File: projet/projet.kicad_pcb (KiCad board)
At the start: 2 copper layers, 2 parts, among them U1 RASPBERRY_PI_PICO

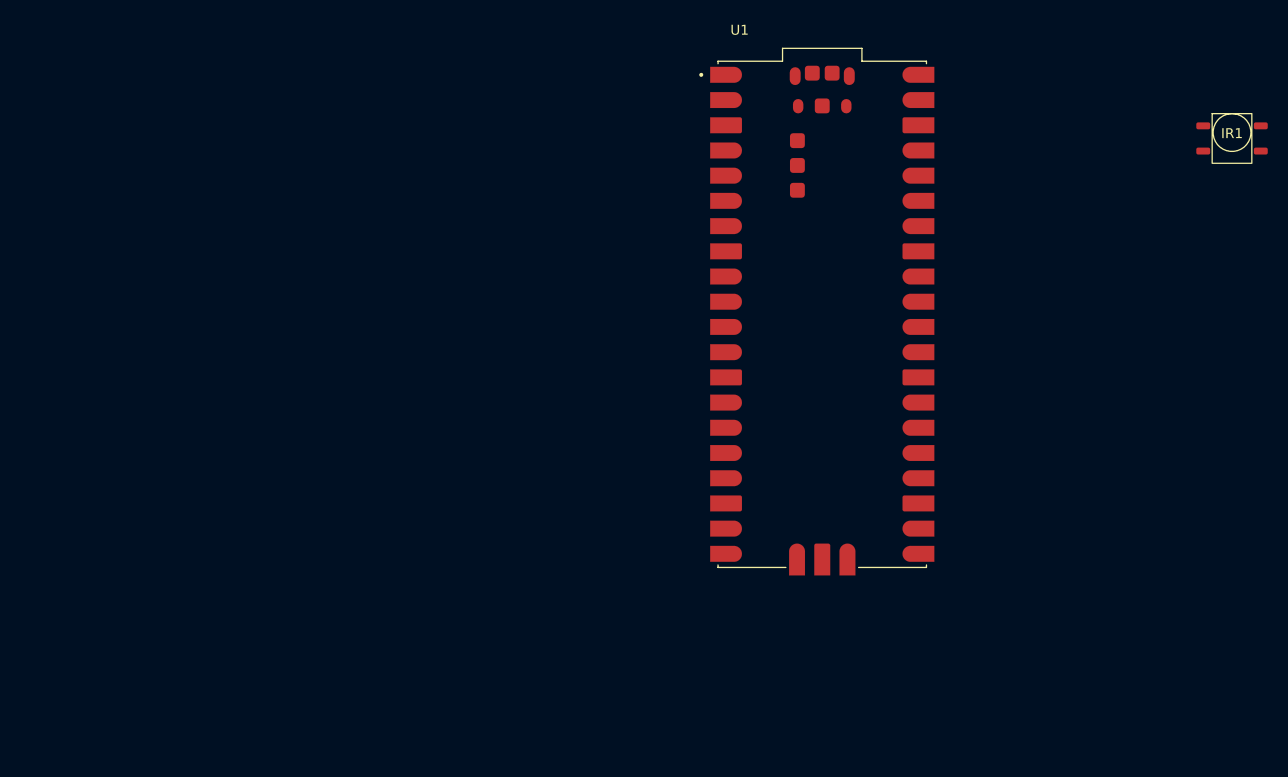
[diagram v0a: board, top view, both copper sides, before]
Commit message: début Routage
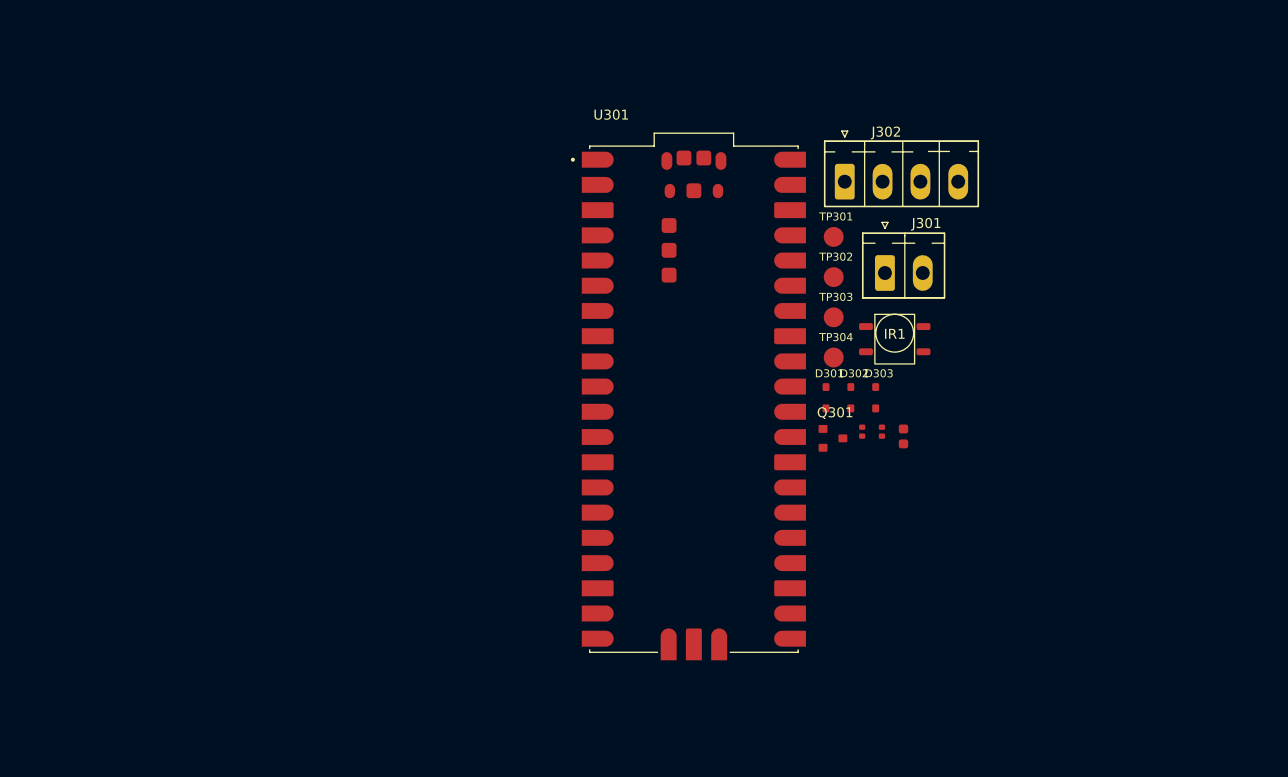
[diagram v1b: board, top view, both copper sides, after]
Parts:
- removed U1: RASPBERRY_PI_PICO, codium_Modules:Raspberry-Pi-Pico
- added C301: 10uF 10V, codium_Basics:C0603, F.Cu at (139.0, 87.8)
- added D301: TVS 5V, codium_Basics:SOD323_NP, F.Cu at (131.2, 83.8)
- added D302: TVS 5V, codium_Basics:SOD323_NP, F.Cu at (133.7, 83.8)
- added D303: TVS 5V, codium_Basics:SOD323_NP, F.Cu at (136.2, 83.8)
- added J301: EMB_P3.81_1x02_VERTICAL, codium_Connectors:Conn_THT_3.81_2x1_Vertical, F.Cu at (137.1, 71.3)
- added J302: EMB_P3.81_1x04_VERTICAL, codium_Connectors:Conn_THT_3.81_4x1_Vertical, F.Cu at (133.1, 62.1)
- added Q301: MOS P 20V 2A, codium_Basics:SOT23, F.Cu at (131.9, 87.9)
- added R301: 100R, codium_Basics:R0402, F.Cu at (134.8, 87.3)
- added R302: 100k, codium_Basics:R0402, F.Cu at (136.8, 87.3)
- added TP301: TestGND, codium_Pads:TestPoint_Pad_D2.0mm, F.Cu at (132.0, 67.7)
- added TP302: TestVCC, codium_Pads:TestPoint_Pad_D2.0mm, F.Cu at (132.0, 71.7)
- added TP303: TestCapteur, codium_Pads:TestPoint_Pad_D2.0mm, F.Cu at (132.0, 75.8)
- added TP304: TestLED, codium_Pads:TestPoint_Pad_D2.0mm, F.Cu at (132.0, 79.8)
- added U301: Raspberry-Pi-Pico_Linked, codium_Modules:Raspberry-Pi-Pico, F.Cu at (117.9, 84.0)
- moved IR1 39.5 mm to (138.1, 78.0)
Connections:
- net Net-(IR1-GND-Pad1) renamed GND
- IR1 pad 3: unconnected-(IR1-OUT-Pad3) -> lecteur_ir_13
- IR1 pad 4: unconnected-(IR1-VCC-Pad4) -> Net-(IR1-VCC)

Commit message: démarrage routage et installations des ports
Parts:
- added C302: 10uF 10V, codium_Basics:C0603, F.Cu at (91.6, 92.0)
- moved Q301 61.1 mm to (79.5, 56.5)
- moved J302 54.8 mm to (96.5, 102.9), turned to 180 degrees
- moved U301 54.2 mm to (64.0, 78.5)
- moved J301 50.2 mm to (89.2, 56.5)
- moved TP302 49.7 mm to (84.6, 56.5)
- moved TP304 48.0 mm to (86.8, 96.0)
- moved D301 46.2 mm to (91.0, 61.0), turned to 90 degrees
- moved D303 45.8 mm to (91.6, 94.2), turned to -90 degrees
- moved D302 43.9 mm to (91.5, 96.0), turned to 90 degrees
- moved TP301 36.2 mm to (97.6, 56.4)
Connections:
- U301 pad A: unconnected-(U301-USB_SHIELD-PadA) -> GND
- U301 pad B: unconnected-(U301-USB_SHIELD-PadA)_2 -> GND
- U301 pad C: unconnected-(U301-USB_SHIELD-PadA)_3 -> GND
- U301 pad D: unconnected-(U301-USB_SHIELD-PadA)_1 -> GND
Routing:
- net +5V: track 0.00 -> 95.0 mm
- net ruban_led_7: track 0.00 -> 84.4 mm
- net GND: track 0.00 -> 80.3 mm, vias 0 -> 12
- net vbus: track 0.00 -> 5.30 mm
- net vsys: track 0.00 -> 5.03 mm
- added copper zone on B.Cu, net GND
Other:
- board outline added: 50 x 70 mm

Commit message: Première version carte complète
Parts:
- added F301: 1.1A, codium_Basics:R1812L, F.Cu at (84.6, 62.9)
- moved IR1 55.8 mm to (82.8, 70.8)
- moved R302 50.2 mm to (86.8, 84.0), turned to 90 degrees
- moved C301 49.9 mm to (90.1, 78.2), turned to 90 degrees
- moved TP303 49.2 mm to (82.8, 75.6)
- moved R301 44.5 mm to (90.8, 81.0)
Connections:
- C302 pad 1: +5V -> Net-(IR1-VCC)
- D301 pad 1: +5V -> Net-(D301-A1)
- D303 pad 2: +5V -> Net-(IR1-VCC)
- J301 pad 1: +5V -> Net-(D301-A1)
- J302 pad 4: +5V -> Net-(IR1-VCC)
- Q301 pad 3: +5V -> Net-(IR1-VCC)
- R301 pad 2: +5V -> Net-(IR1-VCC)
- R302 pad 2: +5V -> Net-(IR1-VCC)
- TP302 pad 1: +5V -> Net-(D301-A1)
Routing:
- net Net-(IR1-VCC): track 0.00 -> 118.9 mm
- net +5V: track 95.0 -> 0.00 mm
- net lecteur_ir_13: track 0.00 -> 73.0 mm
- net Net-(D301-A1): track 0.00 -> 17.4 mm
- net GND: track 80.3 -> 86.8 mm, vias 12 -> 14

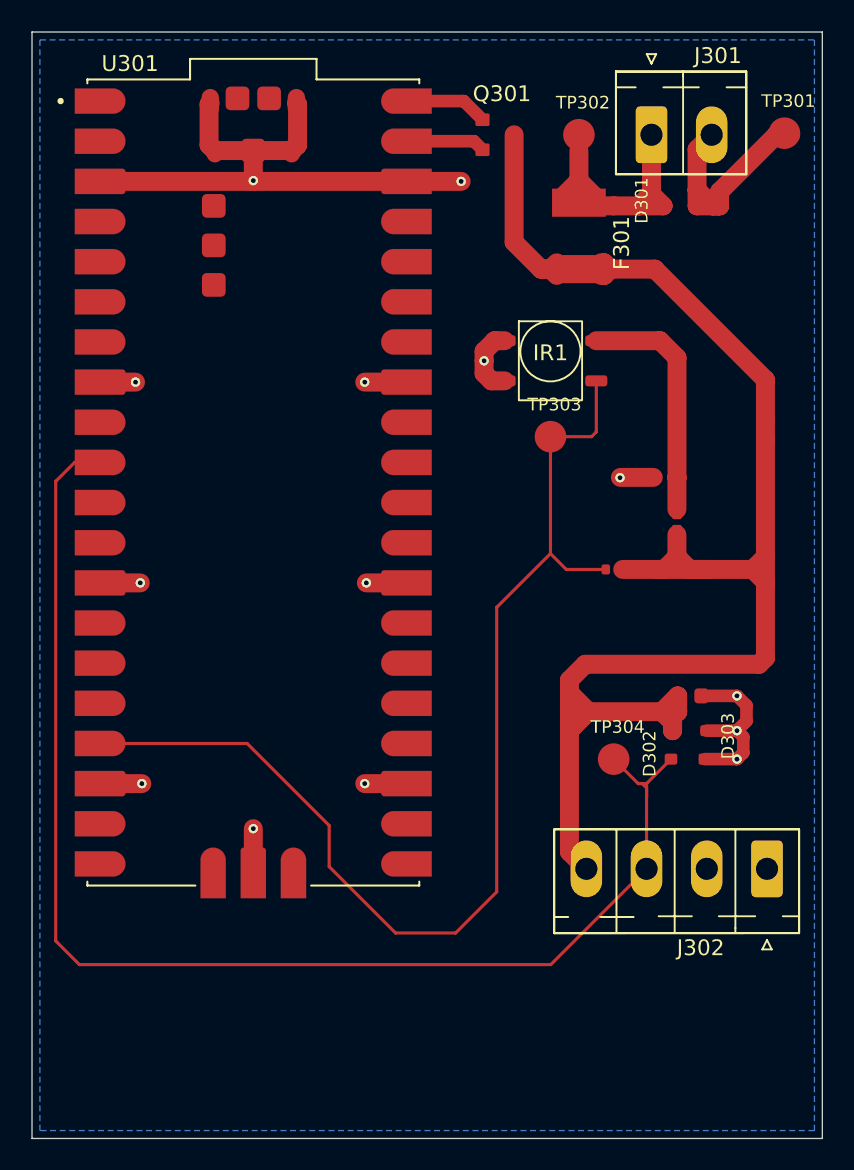
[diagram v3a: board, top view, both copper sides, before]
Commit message: Correctif des pistes et plan de masse au front
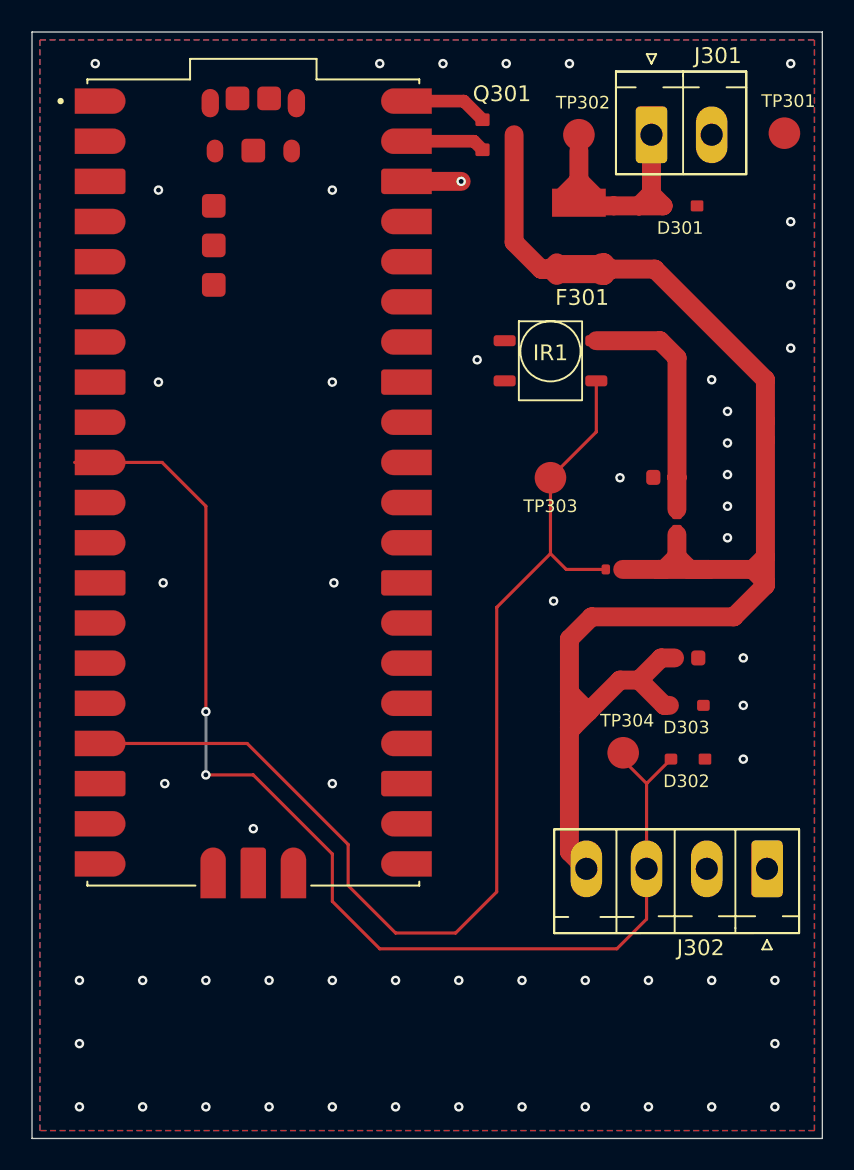
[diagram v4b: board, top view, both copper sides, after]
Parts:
- moved TP303 2.60 mm to (82.8, 78.2)
- moved C302 2.41 mm to (91.4, 89.6)
- moved D303 1.61 mm to (91.4, 92.6)
- moved TP304 0.72 mm to (87.4, 95.6)
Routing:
- net GND: track 86.8 -> 3.49 mm, vias 14 -> 57
- net ruban_led_7: track 84.4 -> 74.7 mm, vias 0 -> 2
- net Net-(IR1-VCC): track 118.9 -> 116.2 mm
- net lecteur_ir_13: track 73.0 -> 71.5 mm
- added copper zone on F.Cu, net GND
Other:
- board text added: "No computer were harmed in the conception of this card"

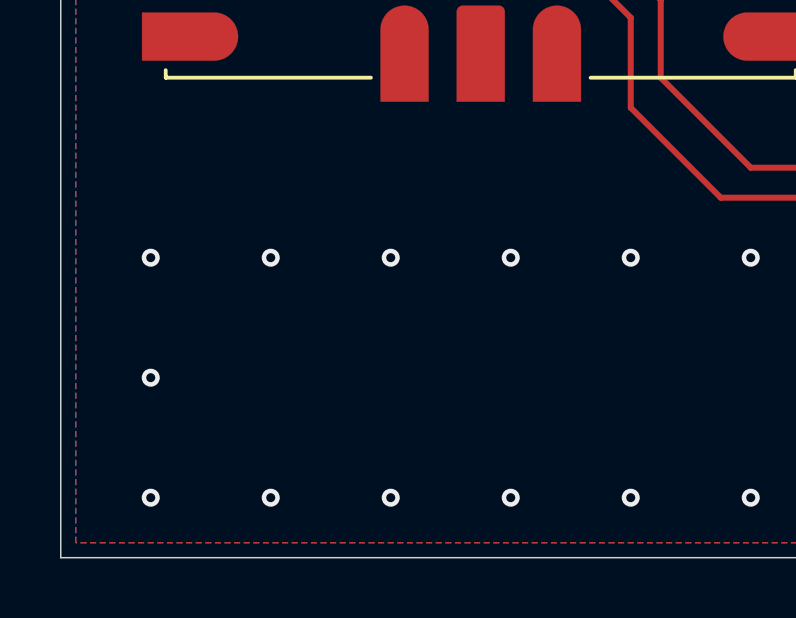
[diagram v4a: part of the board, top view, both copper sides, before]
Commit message: ajout des images sur le^pcb
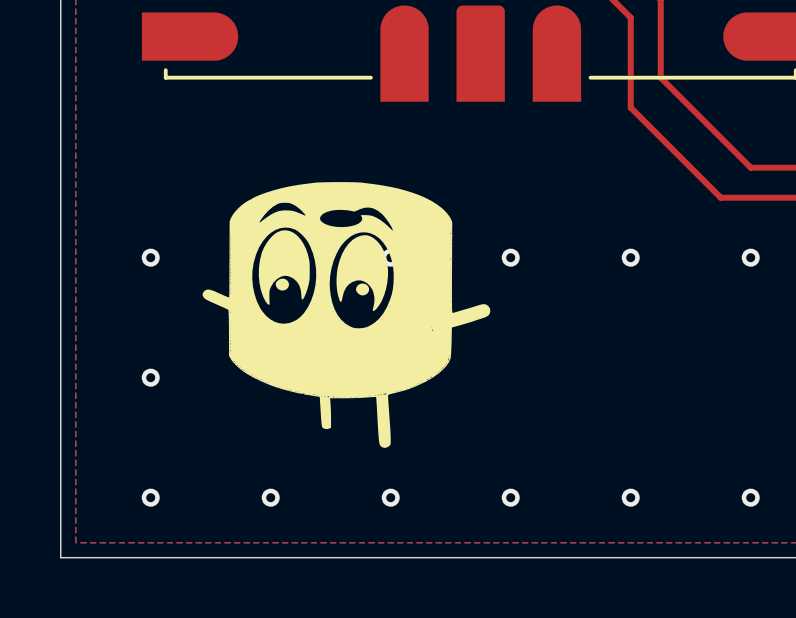
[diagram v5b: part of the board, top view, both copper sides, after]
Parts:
- added G***: LOGO, LOGO, F.Cu at (59.5, 112.0)
- added G***: LOGO, LOGO, B.Cu at (77.0, 68.0)
- added G***: LOGO, LOGO, B.Cu at (75.0, 86.0)

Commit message: Ajout de graphisme et fichiers de fabrications
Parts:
- moved G*** 2.00 mm to (75.0, 68.0)
- moved G*** 1.12 mm to (59.0, 113.0)
- renumbered C302 to C301, C301 to C302, IR1 to IR301, R302 to R301, R301 to R302, TP302 to TP301, TP301 to TP302, TP304 to TP303, TP303 to TP304
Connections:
- C301 pad 1: Net-(IR1-VCC) -> +5V
- C302 pad 2: Net-(IR1-VCC) -> Net-(IR301-VCC)
- D303 pad 2: Net-(IR1-VCC) -> +5V
- F301 pad 2: Net-(IR1-VCC) -> +5V
- IR301 pad 4: Net-(IR1-VCC) -> Net-(IR301-VCC)
- J302 pad 4: Net-(IR1-VCC) -> +5V
- Q301 pad 3: Net-(IR1-VCC) -> +5V
- R301 pad 2: Net-(IR1-VCC) -> +5V
- R302 pad 1: Net-(IR1-VCC) -> Net-(IR301-VCC)
- R302 pad 2: Net-(IR1-VCC) -> +5V
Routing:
- net Net-(IR1-VCC): track 116.2 -> 0.00 mm
- net +5V: track 0.00 -> 101.1 mm
- net Net-(IR301-VCC): track 0.00 -> 15.1 mm
- net GND: vias 57 -> 60
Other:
- board text added: "Design proposed by Gaël Chauvet & Lucas Hyot"

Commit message: Dernière modifs avant vérif externes
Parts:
- added D304: LED GREEN, codium_Leds:LED0805, F.Cu at (96.4, 66.0)
- added D305: LED GREEN, codium_Leds:LED0805, F.Cu at (78.9, 94.0)
- added D306: LED GREEN, codium_Leds:LED0805, F.Cu at (79.1, 90.0)
- added D307: LED GREEN, codium_Leds:LED0805, F.Cu at (79.2, 86.0)
- added R303: 330R, codium_Basics:R0603, F.Cu at (96.4, 62.2)
- added R304: 330R, codium_Basics:R0603, F.Cu at (82.8, 94.0)
- added R305: 330R, codium_Basics:R0603, F.Cu at (82.8, 90.0)
- added R306: 330R, codium_Basics:R0603, F.Cu at (83.1, 86.0)
- moved R302 11.4 mm to (90.2, 69.6), turned to 90 degrees
- moved C302 8.17 mm to (87.7, 70.3), turned to 180 degrees
- moved D302 5.35 mm to (96.8, 96.2)
- moved TP303 5.35 mm to (92.7, 95.8)
- moved TP304 3.20 mm to (86.0, 78.2)
- moved C301 2.60 mm to (94.0, 89.6)
- moved D303 2.60 mm to (94.0, 92.6)
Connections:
- U301 pad 24: unconnected-(U301-GP18-Pad24) -> LED_0
- U301 pad 25: unconnected-(U301-GP19-Pad25) -> LED_1
- U301 pad 26: unconnected-(U301-GP20-Pad26) -> LED_2
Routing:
- net +5V: track 101.1 -> 89.3 mm
- net Net-(IR301-VCC): track 15.1 -> 4.08 mm
- net LED_2: track 0.00 -> 7.25 mm
- net LED_1: track 0.00 -> 5.47 mm
- net LED_0: track 0.00 -> 4.73 mm
- net ruban_led_7: track 74.7 -> 78.1 mm
- net Net-(D307-K): track 0.00 -> 2.26 mm
- net Net-(D304-K): track 0.00 -> 2.14 mm
- net Net-(D305-K): track 0.00 -> 2.12 mm
- net Net-(D306-K): track 0.00 -> 1.99 mm
- net lecteur_ir_13: track 71.5 -> 70.5 mm
- net GND: track 3.49 -> 3.46 mm, vias 60 -> 56
